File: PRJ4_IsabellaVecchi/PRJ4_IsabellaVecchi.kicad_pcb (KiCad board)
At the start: 2 copper layers, 34 parts, among them IC1 STM32L052K8T6, J1 TerminalBateria, J2 Display_OLed, J3 ST-Link, J4 Terminal_SensorUmidadeTerra, J5 Terminal_SensorAmbiente, J6 TerminalPilha, J7 Válvula Solenoide, K1 RT44xxxx, Q1 pnp TO-92 BC307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

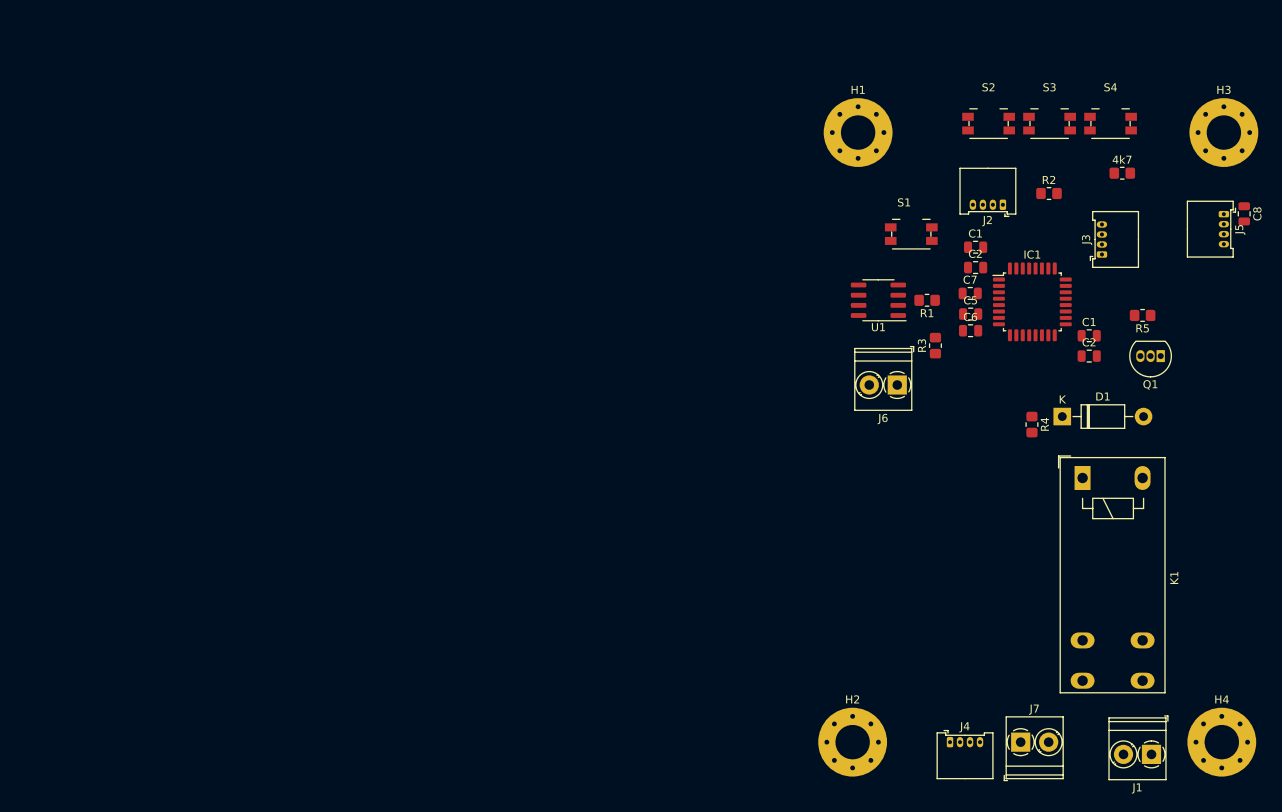
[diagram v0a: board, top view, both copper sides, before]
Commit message: thinking about heat dissipation - pensando na dissipação de calor
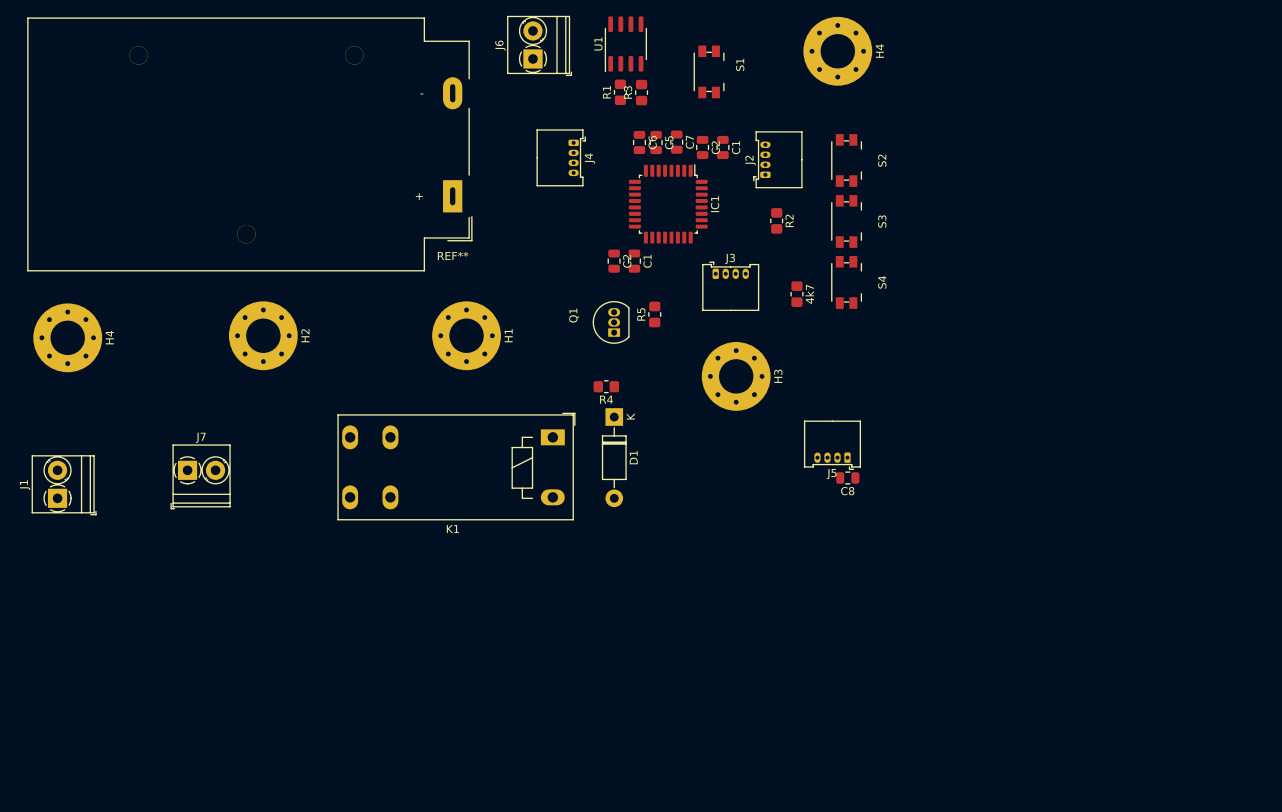
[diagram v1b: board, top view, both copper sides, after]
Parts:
- added H4: MountingHole_Pad, MountingHole:MountingHole_4.3mm_M4_Pad_Via, F.Cu at (170.2, 61.0)
- added REF**: BatteryHolder_MPD_BA9VPC_1xPP3, Battery:BatteryHolder_MPD_BA9VPC_1xPP3, F.Cu at (122.0, 79.1)
- moved H4 152.9 mm to (73.9, 96.8), turned to -90 degrees
- moved J1 140.4 mm to (72.6, 116.8), turned to 90 degrees
- moved J7 109.5 mm to (88.9, 113.3)
- moved H2 89.5 mm to (98.4, 96.5), turned to -90 degrees
- moved J4 88.5 mm to (137.2, 72.4), turned to -90 degrees
- moved Q1 68.4 mm to (142.2, 96.1), turned to 90 degrees
- moved H3 68.2 mm to (157.5, 101.6), turned to -90 degrees
- moved K1 66.4 mm to (134.6, 109.2), turned to 180 degrees
- moved J6 61.1 mm to (132.1, 61.9), turned to 90 degrees
- moved R5 61.0 mm to (147.3, 93.9), turned to 90 degrees
- moved C2 60.6 mm to (142.2, 87.2), turned to -90 degrees
- moved C8 59.5 mm to (171.4, 114.3), turned to 180 degrees
- moved C1 57.6 mm to (144.8, 87.2), turned to -90 degrees
- moved J5 56.0 mm to (171.4, 111.8), turned to 180 degrees
- moved D1 56.0 mm to (142.2, 106.7), turned to -90 degrees
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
